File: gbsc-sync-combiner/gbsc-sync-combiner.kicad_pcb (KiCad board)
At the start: 2 copper layers, 42.8 x 32 mm, 9 parts, among them J1 DB15_Female_HighDensity_Mount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, J2 JST-XH, J3 JST-XH, U1 74LS86

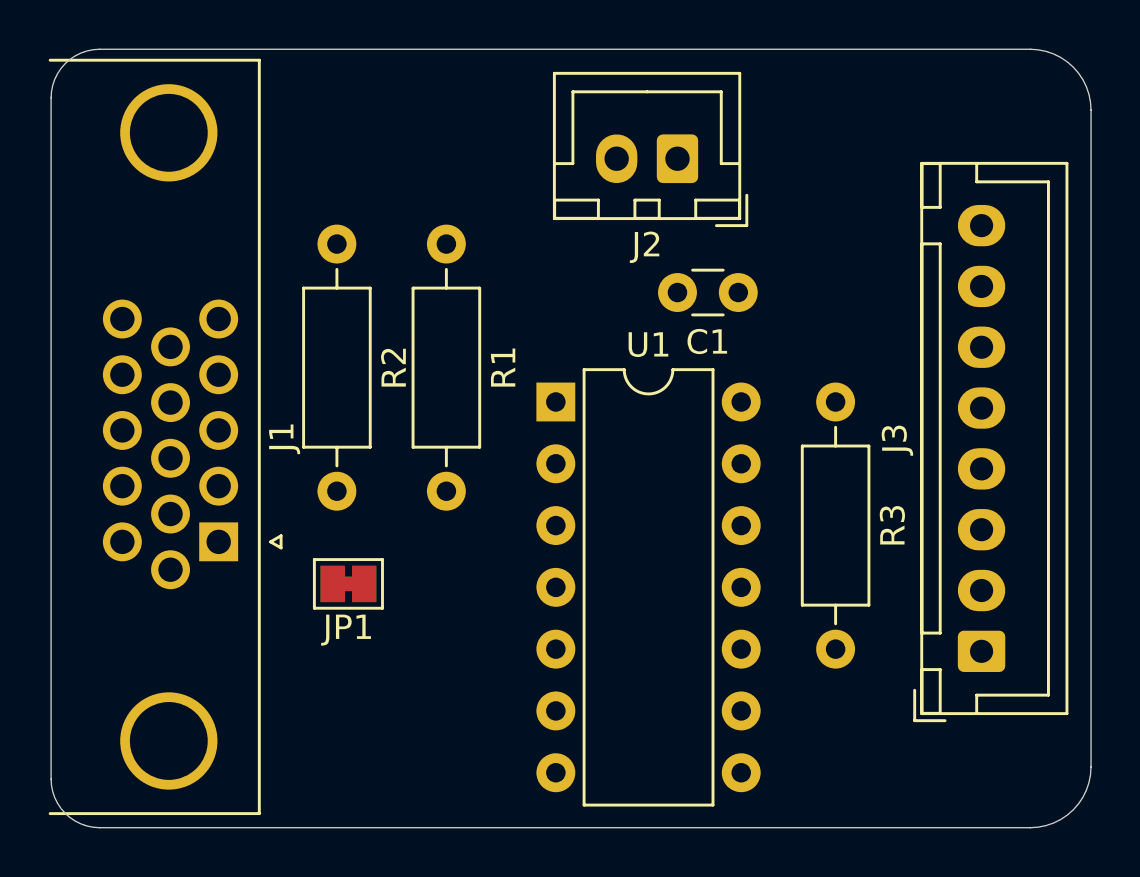
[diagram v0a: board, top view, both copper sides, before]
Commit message: Added mounting holes
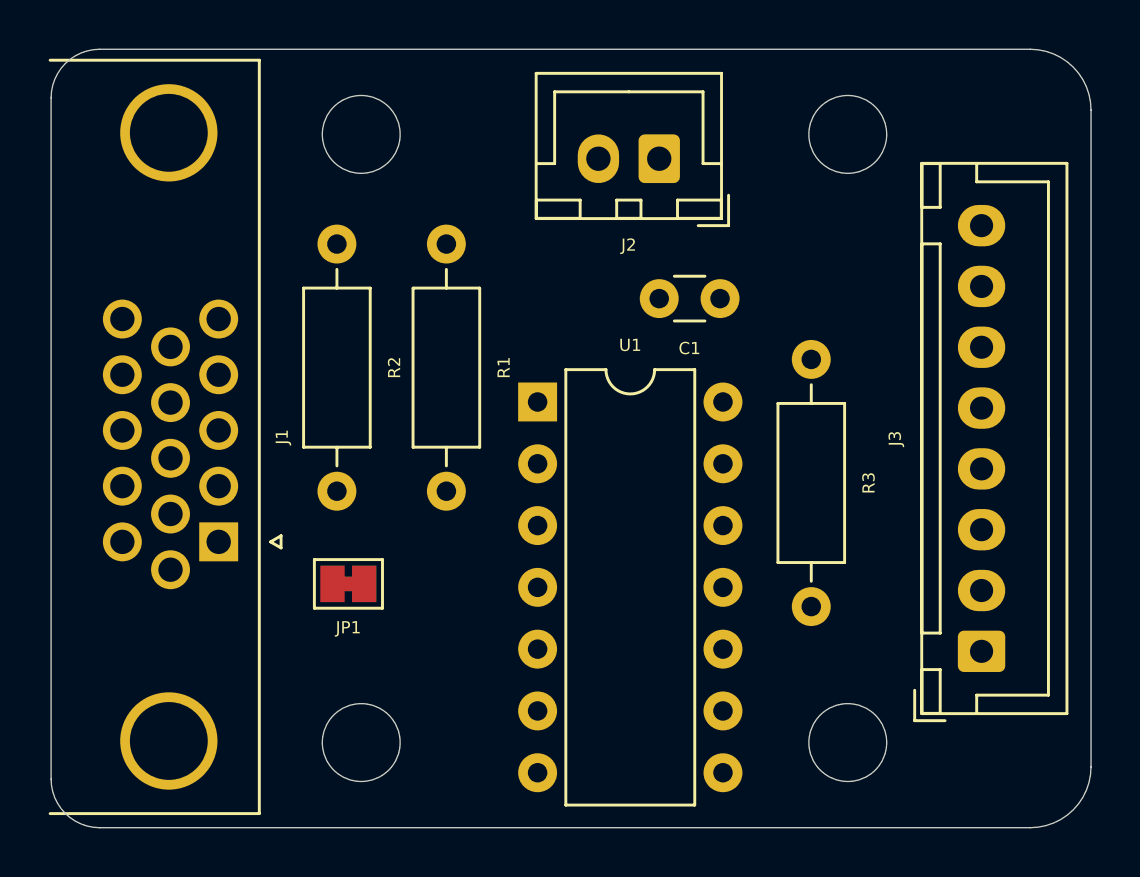
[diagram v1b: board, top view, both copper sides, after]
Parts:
- added H1: MountingHole, MountingHole:MountingHole_3.2mm_M3, F.Cu at (110.0, 60.0)
- added H2: MountingHole, MountingHole:MountingHole_3.2mm_M3, F.Cu at (110.0, 85.0)
- added H3: MountingHole, MountingHole:MountingHole_3.2mm_M3, F.Cu at (130.0, 85.0)
- added H4: MountingHole, MountingHole:MountingHole_3.2mm_M3, F.Cu at (130.0, 60.0)
- moved R3 2.02 mm to (128.5, 69.2)
- moved C1 0.79 mm to (124.8, 66.8)
- moved J2 0.75 mm to (122.2, 61.0)
- moved U1 0.75 mm to (117.2, 71.0)
